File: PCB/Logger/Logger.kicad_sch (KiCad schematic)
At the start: 23 parts, among them J2 USB-C-Socket-V, J3 USB-PROG, J5 Conn_01x05, J5 POWER, J6 DM3AT-SF-PEJM5, J8 Shelly, U1 MD8942, U10 ESP32-S3-MINI-1, U5 QR

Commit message: More work
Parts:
- removed C1: 10uF 50V, RevK:C_0603_, symbol RevK:Hidden
- removed C7: 10uF 6.3V, RevK:C_0603_, symbol RevK:Hidden
- removed C9: 100nF, RevK:C_0603_, symbol RevK:Hidden
- removed D1: D, RevK:D_1206, symbol Device:D
- removed J5: POWER, RevK:PTSM-HH1-2-RA, symbol RevK:PowerIn
- removed L2: 10uH, RevK:L_4x4_, symbol RevK:Hidden
- removed R1: 124k, RevK:R_0402_, symbol RevK:Hidden
- removed R2: 40k2, RevK:R_0402_, symbol RevK:Hidden
- removed R3: 1M, RevK:R_0402_, symbol RevK:Hidden
- removed U1: MD8942, RevK:SOT-23-6-MD8942, symbol RevK:MD89420-RegBlock
- added C12: 4.7uF/50V, RevK:C_0805, symbol Device:C
- added C28: C_Polarized, Capacitor_Tantalum_SMD:CP_EIA-7343-31_Kemet-D, symbol Device:C_Polarized
- added D27 (x4): ~, RevK:DFN1006-2L, symbol RevK:ES05D1MC10
- added D4: MBR0530, RevK:D_SOD-123, symbol Device:D_Schottky
- added J3: JST-PH-SM3-TB, Connector_JST:JST_PH_S2B-PH-SM4-TB_1x02-1MP_P2.00mm_Horizontal, symbol Connector_Generic:Conn_01x02
- added Q1: C179347, RevK:SOT-323_SC-70, symbol Device:Q_PMOS_GSD
- added Q4: CJ2301, RevK:SOT-23, symbol Transistor_FET:BSS83P
- added R1, R14, R15: 10K, RevK:R_0402, symbol Device:R
- added R12, R13: 100K, RevK:R_0402, symbol Device:R
- added U1: TP4054, RevK:SOT-23-5, symbol RevK:TP4054
- added U2: ME6211C33M5G-N, RevK:SOT-23-5, symbol Regulator_Linear:TLV70033_SOT23-5
- J5: now left out of the parts list
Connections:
- net GND: now also J6.9 (SHIELD), C12.2, C28.2, D27.1, D27.1, D27.1, D27.1, J3.1 (Pin_1), R13.2, R14.2, R15.1, U1.2 (VSS), U2.2 (GND)
- net GPSRX: now also D27.2
- net GPSTICK: now also D27.2
- net GPSTX: now also D27.2
- net VBUS: now also C28.1, D4.2 (A), Q4.1 (G), R14.1, U1.4 (VDD)
- net STAT: now reaches U10.29 (GPIO34)
- net STAT: now also U1.1 (STAT)
- net ADC: now reaches U10.31 (GPIO35)
- net ADC: now also R12.2, R13.1
- net GPSPWR: now reaches U10.32 (GPIO36)
- net GPSPWR: now also Q1.1 (G), R1.2
- net +3V3 renamed +3.3V
- net +3.3V: now also C12.1, Q1.2 (S), R1.1, U2.5 (OUT); no longer J5.5 (Pin_5)
- new net: D4.1 (K), Q4.2 (S), U2.1 (IN), U2.3 (EN)
- new net: R15.2, U1.5 (PROG)
- new net VBAT: J3.2 (Pin_2), Q4.3 (D), R12.1, U1.3 (VBAT)
- new net VGPS: D27.2, J5.5 (Pin_5), Q1.3 (D)
- no-connect marks 2 -> 35
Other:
- note added: "Add accelerometer"
- note added: "Draw MicroSD for C393941"
- moved on the sheet: D4, J2, J3, R2, R3

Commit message: Ready to order
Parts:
- removed J6: DM3AT-SF-PEJM5, Connector_Card:microSD_HC_Hirose_DM3AT-SF-PEJM5, symbol Connector:Micro_SD_Card
- removed Logo2: AJK, RevK:AJK, symbol RevK:AJK
- removed U5: QR, RevK:QR-SS, symbol RevK:QR
- added C12: 4.7uF/50V, RevK:C_0805, symbol Device:C
- added C246 (x14): 100nF, RevK:C_0402, symbol Device:C
- added D4 (x13): XL-1010RGBC-WS2812B, RevK:SMD1010, symbol RevK:WS2812B-1mm
- added J6: TF_PUSH, RevK:TF_PUSH, symbol RevK:TF_PUSH
- added PCB1: 70x70, RevK:PCB7070, symbol RevK:PCB
- added U2: ~, Package_LGA:LGA-16_3x3mm_P0.5mm_LayoutBorder3x5y, symbol RevK:LIS3DHTR
- added V1, V3, V4, V6: ~, RevK:VCUT70N, symbol RevK:VCUT
- J3: value JST-PH-SM3-TB -> JST-PH-SM4-TB; footprint Connector_JST:JST_PH_S2B-PH-SM4-TB_1x02-1MP_P2.00mm_Horizontal -> RevK:JST_PH_S2B-PH-SM4-TB_1x02-1MP_P2.00mm_Horizontal
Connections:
- net +3.3V: now also C246.1, C246.1, C246.1, C246.1, C246.1, C246.1, C246.1, C246.1, C246.1, C246.1, C246.1, C246.1, C246.1, C246.1, D4.2 (+), D4.2 (+), D4.2 (+), D4.2 (+), D4.2 (+), D4.2 (+), D4.2 (+), D4.2 (+), D4.2 (+), D4.2 (+), D4.2 (+), D4.2 (+), D4.2 (+)
- net GND: now also C12.2, C246.2, C246.2, C246.2, C246.2, C246.2, C246.2, C246.2, C246.2, C246.2, C246.2, C246.2, C246.2, C246.2, C246.2, D4.3 (-), D4.3 (-), D4.3 (-), D4.3 (-), D4.3 (-), D4.3 (-), D4.3 (-), D4.3 (-), D4.3 (-), D4.3 (-), D4.3 (-), D4.3 (-), D4.3 (-), J6.6 (VSS), J6.S (SHIELD), U2.10 (RES), U2.12 (GND), U2.5 (GND)
- net GPSRX: now also U10.11 (GPIO7); no longer U10.36 (GPIO40)
- net GPSTICK: now also U10.7 (GPIO3); no longer U10.37 (GPIO41)
- net GPSTX: now also U10.9 (GPIO5); no longer U10.33 (GPIO37)
- net RGB: now also U10.29 (GPIO34); no longer U10.28 (GPIO33)
- net STAT: now also U10.28 (GPIO33); no longer U10.29 (GPIO34)
- net at D4.1 (O): now also D4.4 (I)
- net SDSS: now reaches U10.12 (GPIO8)
- net SDSS: now also J6.2 (DAT3/CD)
- net SDMOSI: now reaches U10.13 (GPIO9)
- net SDMOSI: now also J6.3 (CMD)
- net SDSCK: now reaches U10.14 (GPIO10)
- net SDSCK: now also J6.5 (CLK)
- net SDCD: now reaches U10.15 (GPIO11)
- net SDCD: now also J6.9 (CD)
- net SDMISO: now reaches U10.16 (GPIO12)
- net SDMISO: now also J6.7 (DAT0)
- net ACCSDA: now reaches U10.17 (GPIO13)
- net ACCSDA: now also U2.6 (SDA/SDI/SDO)
- net ACCSCL: now reaches U10.18 (GPIO14)
- net ACCSCL: now also U2.4 (SCL/SPC)
- net PWR: now reaches U10.19 (GPIO15)
- net PWR: now also Q1.1 (G), R1.2
- removed net GPSPWR: Q1.1 (G), R1.2, U10.32 (GPIO36)
- net VGPS renamed SPWR
- net SPWR: now also C12.1, J6.4 (VDD), U2.1 (VDD_IO), U2.14 (VDD), U2.8 (CS)
- new net: D4.1 (O), D4.4 (I) (x12)
- no-connect marks 35 -> 28
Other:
- note removed: "Add accelerometer"
- note removed: "Draw MicroSD for C393941"
- moved on the sheet: D4, Q1, R1

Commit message: Ready to order
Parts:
- added C1 (x2): 100nF, RevK:C_0402, symbol Device:C
- added C2 (x2): 22uF, RevK:C_0603, symbol Device:C
- added D27: ~, RevK:DFN1006-2L, symbol RevK:ES05D1MC10
- added R12: 100K 1%, RevK:R_0402, symbol Device:R
- J3: symbol Connector_Generic:Conn_01x02 -> Connector_Generic:Conn_01x04
- J5: symbol Connector_Generic:Conn_01x05 -> Connector_Generic:Conn_01x07; now in the parts list
- R12, R13: value 100K -> 100K 1%
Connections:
- net +3.3V: now also C1.1, C2.1; no longer C246.1, C246.1, C246.1, C246.1, C246.1, C246.1, C246.1, C246.1, C246.1, C246.1, C246.1, C246.1, C246.1, C246.1, D4.2 (+), D4.2 (+), D4.2 (+), D4.2 (+), D4.2 (+), D4.2 (+), D4.2 (+), D4.2 (+), D4.2 (+), D4.2 (+), D4.2 (+), D4.2 (+), D4.2 (+), D4.2 (+)
- net ADC: now also U2.16 (ADC1); no longer U10.31 (GPIO35)
- net GND: now also J3.3 (Pin_3), J3.4 (Pin_4), J5.6 (Pin_6), J5.7 (Pin_7), C1.2, C1.2, C2.2, C2.2, D27.1
- net SPWR: now also C246.1, C246.1, C246.1, C246.1, C246.1, C246.1, C246.1, C246.1, C246.1, C246.1, C246.1, C246.1, C246.1, C246.1, D4.2 (+), D4.2 (+), D4.2 (+), D4.2 (+), D4.2 (+), D4.2 (+), D4.2 (+), D4.2 (+), D4.2 (+), D4.2 (+), D4.2 (+), D4.2 (+), D4.2 (+), D4.2 (+), C1.1, C2.1
- net VBAT: now also D27.2, R12.1; no longer R12.1
- new net: R12.1, R12.2

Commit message: Ordered
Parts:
- J5: now left out of the parts list
- R12, R13: LCSC Part # (none) -> C5139597
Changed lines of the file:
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@@
       (effects (font (size 1.27 1.27)) hide)
     )
+    (property "LCSC Part #" "C5139597" (at 247.65 41.275 90)
+      (effects (font (size 1.27 1.27)) hide)
+    )
     (pin "1")
     (pin "2")
@@
   )
   (symbol (lib_id "Connector_Generic:Conn_01x07") (at 48.895 125.73 0) (mirror y) (unit 1)
-    (in_bom yes) (on_board yes) (dnp no) (fields_autoplaced)
+    (in_bom no) (on_board yes) (dnp no) (fields_autoplaced)
     (property "Reference" "J5" (at 48.895 112.6957 0)
       (effects (font (size 1.27 1.27)))
@@
       (effects (font (size 1.27 1.27)) hide)
     )
+    (property "LCSC Part #" "C5139597" (at 247.65 33.655 90)
+      (effects (font (size 1.27 1.27)) hide)
+    )
     (pin "1")
     (pin "2")
@@
       (effects (font (size 1.27 1.27)) hide)
     )
+    (property "LCSC Part #" "C5139597" (at 247.65 26.035 90)
+      (effects (font (size 1.27 1.27)) hide)
+    )
     (pin "1")
     (pin "2")
@@
   (symbol (lib_id "Connector_Generic:Conn_01x04") (at 137.16 67.945 0) (unit 1)
     (in_bom yes) (on_board yes) (dnp no)
-    (property "Reference" "J3" (at 137.16 65.405 0)
+    (property "Reference" "J3" (at 137.16 76.835 0)
       (effects (font (size 1.27 1.27)))
     )

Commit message: Reverse tantalum FFS
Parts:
- C28: JLCPCB Rotation Offset (none) -> 180
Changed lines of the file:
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@@
+      (effects (font (size 1.27 1.27)) hide)
+    )
+    (property "JLCPCB Rotation Offset" "180" (at 257.175 61.595 0)
       (effects (font (size 1.27 1.27)) hide)
     )

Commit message: SS
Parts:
- C28: footprint Capacitor_Tantalum_SMD:CP_EIA-7343-31_Kemet-D -> RevK:CP_EIA-7343-31_Kemet-D
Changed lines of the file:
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@@
       (effects (font (size 1.27 1.27)) (justify right))
     )
-    (property "Footprint" "Capacitor_Tantalum_SMD:CP_EIA-7343-31_Kemet-D" (at 256.2098 57.785 0)
+    (property "Footprint" "RevK:CP_EIA-7343-31_Kemet-D" (at 256.2098 57.785 0)
       (effects (font (size 1.27 1.27)) hide)
     )

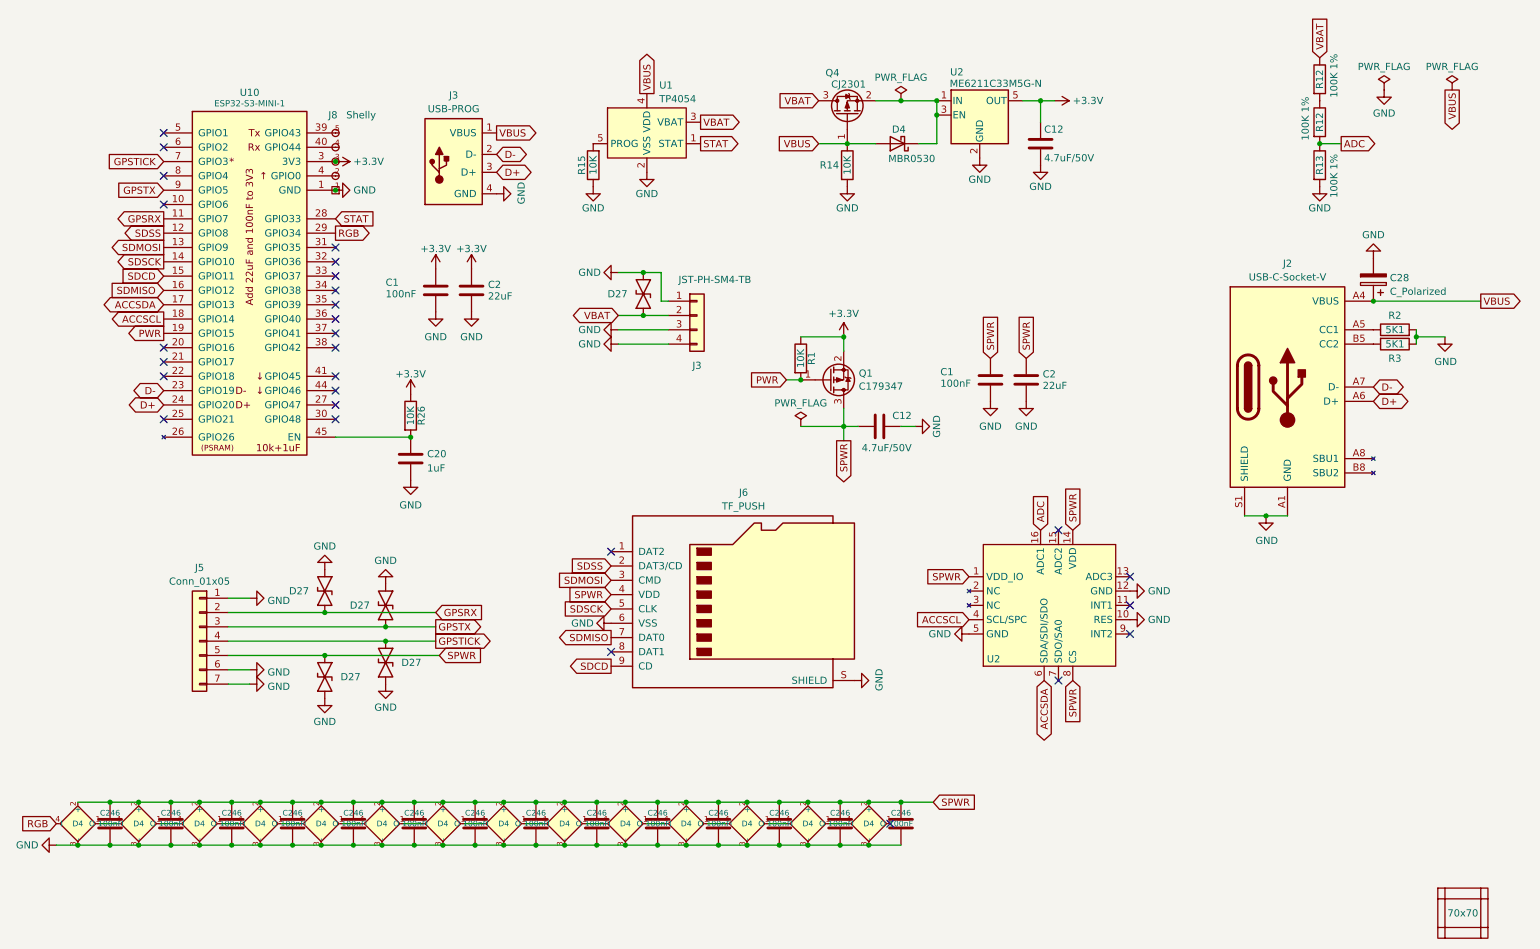
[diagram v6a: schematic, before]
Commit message: Reworked, more LEDs, etc
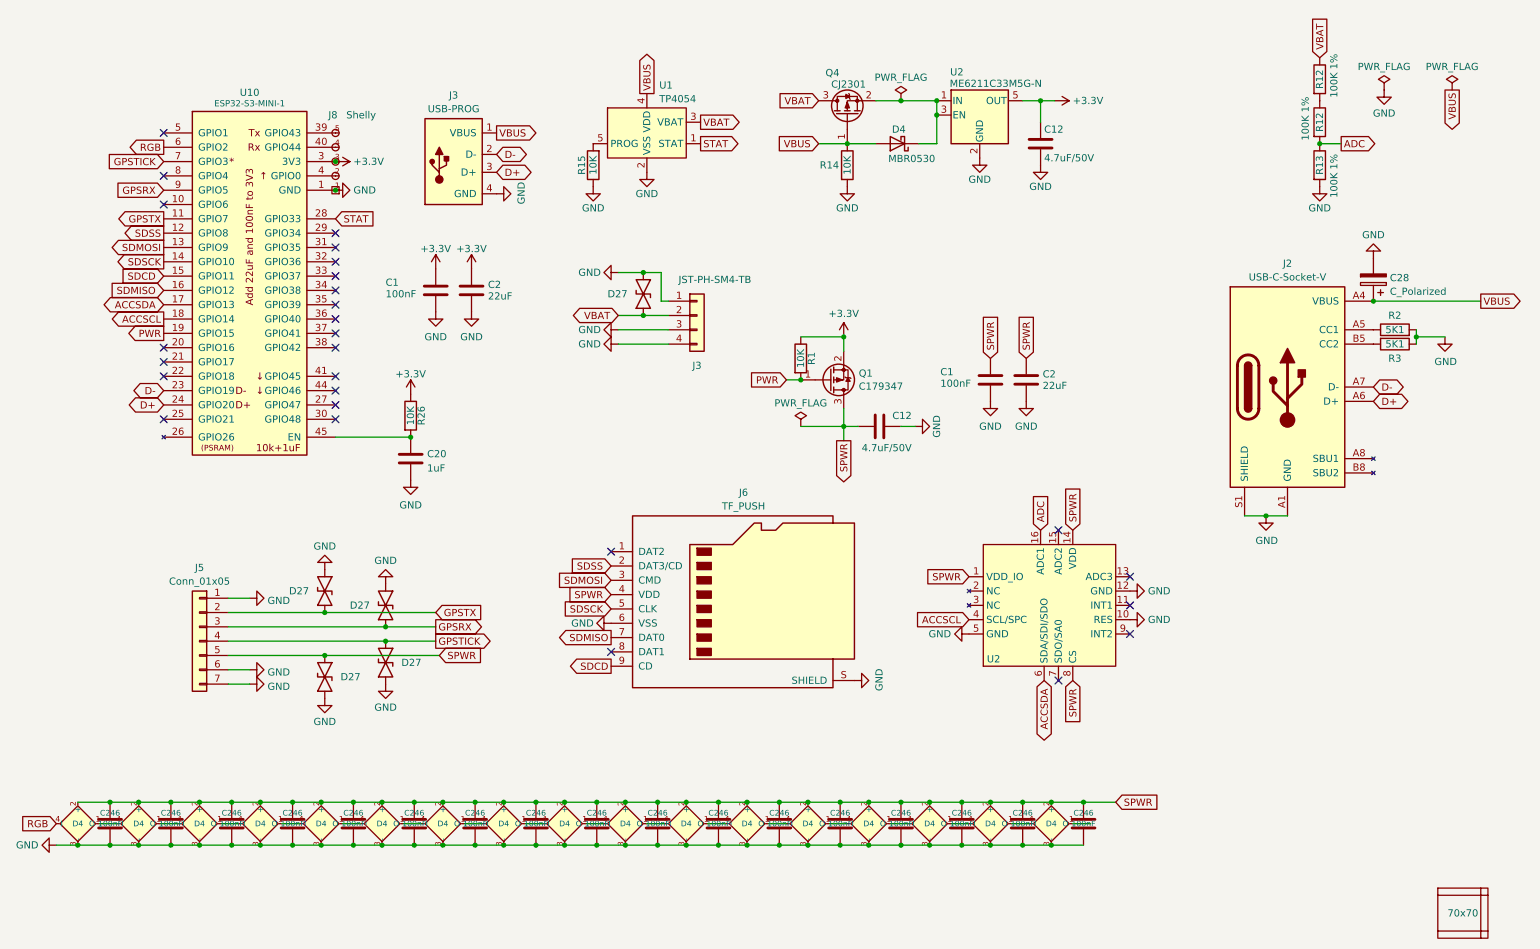
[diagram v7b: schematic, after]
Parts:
- removed V4: ~, RevK:VCUT70N, symbol RevK:VCUT
- added C246 (x3): 100nF, RevK:C_0402, symbol Device:C
- added D4 (x3): XL-1010RGBC-WS2812B, RevK:SMD1010, symbol RevK:WS2812B-1mm
- Q1: footprint RevK:SOT-323_SC-70 -> RevK:SOT-23; LCSC Part # C179347 -> C3034
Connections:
- net GND: now also C246.2, C246.2, C246.2, D4.3 (-), D4.3 (-), D4.3 (-)
- net GPSRX: now also D27.2, J5.3 (Pin_3), U10.9 (GPIO5); no longer D27.2, J5.2 (Pin_2), U10.11 (GPIO7)
- net GPSTX: now also D27.2, J5.2 (Pin_2), U10.11 (GPIO7); no longer D27.2, J5.3 (Pin_3), U10.9 (GPIO5)
- net RGB: now also U10.6 (GPIO2); no longer U10.29 (GPIO34)
- net SPWR: now also C246.1, C246.1, C246.1, D4.2 (+), D4.2 (+), D4.2 (+)
- net at D4.1 (O): now also D4.4 (I)
- new net: D4.1 (O), D4.4 (I) (x2)
- no-connect marks 28 -> 27

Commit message: Manual
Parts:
- Q1: JLCPCB Rotation Offset (none) -> 180
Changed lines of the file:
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@@
+      (effects (font (size 1.27 1.27)) hide)
+    )
+    (property "JLCPCB Rotation Offset" "180" (at 160.655 79.375 0)
       (effects (font (size 1.27 1.27)) hide)
     )
